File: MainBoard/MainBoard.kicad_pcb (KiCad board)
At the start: 6 copper layers, 45 x 45 mm, 4 parts, among them J2 USB4110-GF-A, J3 M55-7104042R

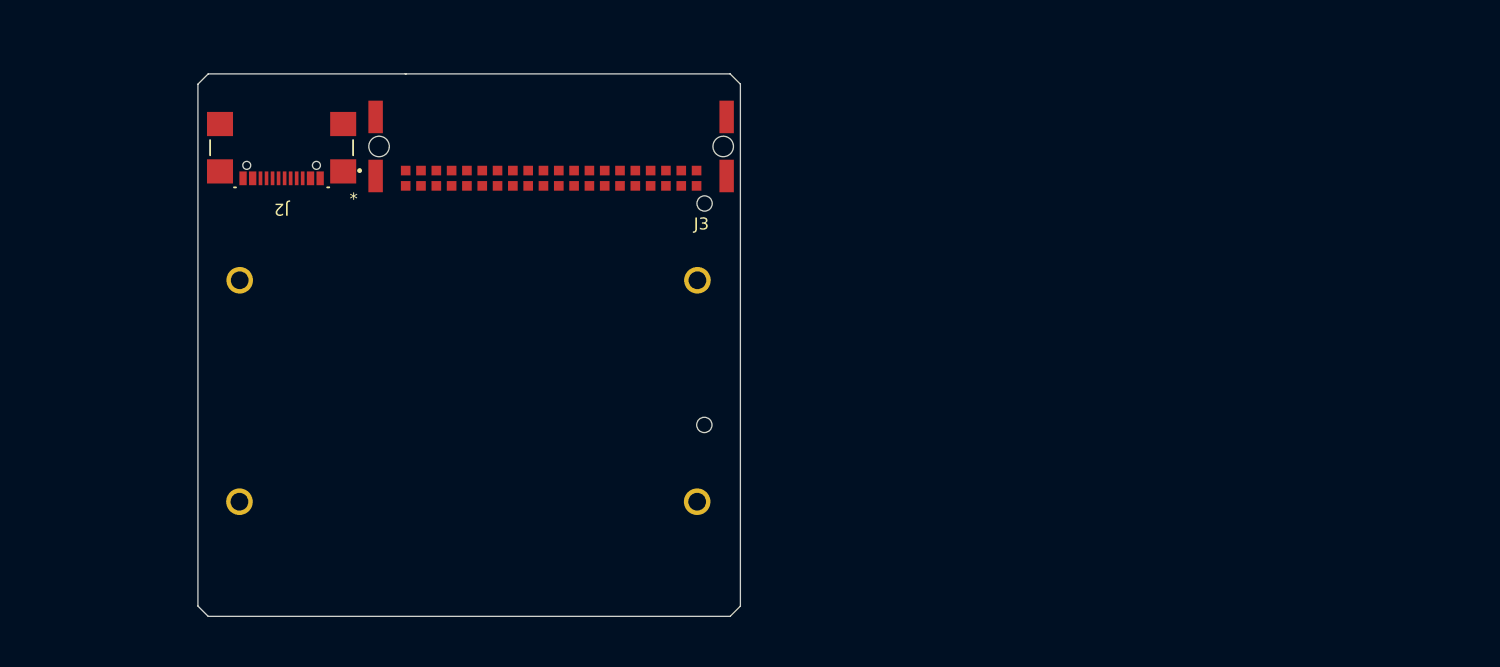
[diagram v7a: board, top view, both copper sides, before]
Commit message: Did some placement
Did most the caps for MCU, general placement for fill zones
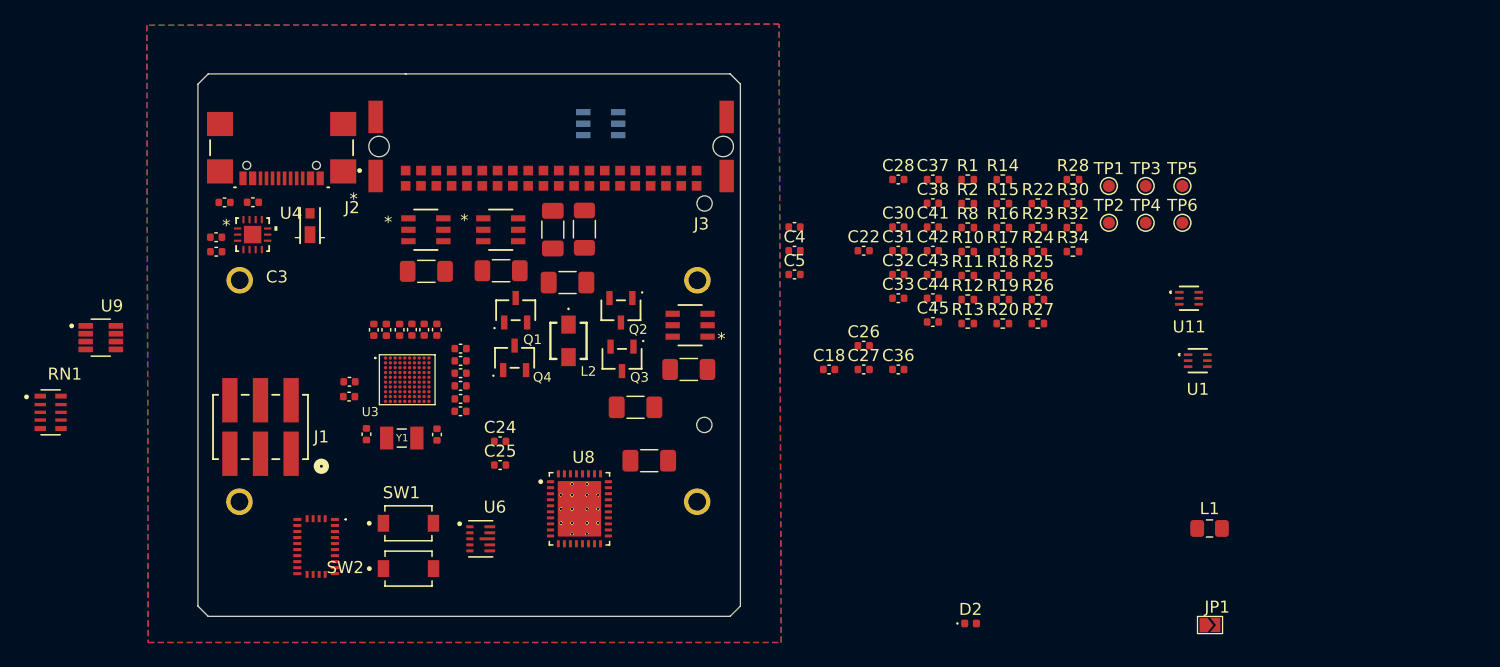
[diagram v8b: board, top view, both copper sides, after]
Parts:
- added C1: 1uF, Capacitor_SMD:C_0402_1005Metric, F.Cu at (70.9, 55.3)
- added C10: 4.7uF, Capacitor_SMD:C_0402_1005Metric, F.Cu at (85.0, 63.0)
- added C11: 4.7uF, Capacitor_SMD:C_0402_1005Metric, F.Cu at (87.2, 63.0)
- added C12: 100nF, Capacitor_SMD:C_0402_1005Metric, F.Cu at (89.2, 63.0)
- added C13: 100nF, Capacitor_SMD:C_0402_1005Metric, F.Cu at (88.2, 63.0)
- added C14: 100nF, Capacitor_SMD:C_0402_1005Metric, F.Cu at (91.2, 64.5)
- added C15: 100nF, Capacitor_SMD:C_0402_1005Metric, F.Cu at (82.0, 67.3)
- added C16: 1uF, Capacitor_SMD:C_0402_1005Metric, F.Cu at (84.0, 63.0)
- added C17: 100nF, Capacitor_SMD:C_0402_1005Metric, F.Cu at (81.9, 68.5)
- added C18: 10uF, Capacitor_SMD:C_0402_1005Metric, F.Cu at (121.8, 66.3)
- added C19: 1uF, Capacitor_SMD:C_0402_1005Metric, F.Cu at (91.2, 65.6)
- added C2: 100nF, Capacitor_SMD:C_0402_1005Metric, F.Cu at (70.9, 56.5)
- added C20: 100nF, Capacitor_SMD:C_0402_1005Metric, F.Cu at (86.1, 63.0)
- added C21: 100nF, Capacitor_SMD:C_0402_1005Metric, F.Cu at (91.2, 66.6)
- added C22: 100nF, Capacitor_SMD:C_0402_1005Metric, F.Cu at (124.6, 56.4)
- added C23: 100nF, Capacitor_SMD:C_0402_1005Metric, F.Cu at (91.2, 67.6)
- added C24: 100nF, Capacitor_SMD:C_0402_1005Metric, F.Cu at (94.5, 72.2)
- added C25: 100nF, Capacitor_SMD:C_0402_1005Metric, F.Cu at (94.5, 74.2)
- added C26: 10uF, Capacitor_SMD:C_0402_1005Metric, F.Cu at (124.6, 64.3)
- added C27: 10uF, Capacitor_SMD:C_0402_1005Metric, F.Cu at (124.6, 66.3)
- added C28: 100nF, Capacitor_SMD:C_0402_1005Metric, F.Cu at (127.5, 50.5)
- added C29: 22pF, Capacitor_SMD:C_0402_1005Metric, F.Cu at (83.4, 71.7)
- added C3: 100nF, Capacitor_SMD:C_0402_1005Metric, F.Cu at (118.9, 54.5)
- added C30: 100nF, Capacitor_SMD:C_0402_1005Metric, F.Cu at (127.5, 54.5)
- added C31: 470nF, Capacitor_SMD:C_0402_1005Metric, F.Cu at (127.5, 56.4)
- added C32: 100nF, Capacitor_SMD:C_0402_1005Metric, F.Cu at (127.5, 58.4)
- added C33: 100nF, Capacitor_SMD:C_0402_1005Metric, F.Cu at (127.5, 60.4)
- added C34: 47uF, Capacitor_SMD:C_1206_3216Metric_Pad1.33x1.80mm_HandSolder, F.Cu at (105.7, 69.4)
- added C35: 47uF, Capacitor_SMD:C_1206_3216Metric_Pad1.33x1.80mm_HandSolder, F.Cu at (100.1, 59.1)
- added C36: 4.7uF, Capacitor_SMD:C_0402_1005Metric, F.Cu at (127.5, 66.3)
- added C37: 4.7uF, Capacitor_SMD:C_0402_1005Metric, F.Cu at (130.4, 50.5)
- added C38: 1uF, Capacitor_SMD:C_0402_1005Metric, F.Cu at (130.4, 52.5)
- added C39: 47uF, Capacitor_SMD:C_1206_3216Metric_Pad1.33x1.80mm_HandSolder, F.Cu at (106.8, 73.8)
- added C4: 100nF, Capacitor_SMD:C_0402_1005Metric, F.Cu at (118.9, 56.4)
- added C40: 47uF, Capacitor_SMD:C_1206_3216Metric_Pad1.33x1.80mm_HandSolder, F.Cu at (98.8, 54.7)
- added C41: 100nF, Capacitor_SMD:C_0402_1005Metric, F.Cu at (130.4, 54.5)
- added C42: 100nF, Capacitor_SMD:C_0402_1005Metric, F.Cu at (130.4, 56.4)
- added C43: 100nF, Capacitor_SMD:C_0402_1005Metric, F.Cu at (130.4, 58.4)
- added C44: 470nF, Capacitor_SMD:C_0402_1005Metric, F.Cu at (130.4, 60.4)
- added C45: 100nF, Capacitor_SMD:C_0402_1005Metric, F.Cu at (130.4, 62.3)
- added C46: 22pF, Capacitor_SMD:C_0402_1005Metric, F.Cu at (89.2, 71.7)
- added C5: 100nF, Capacitor_SMD:C_0402_1005Metric, F.Cu at (118.9, 58.4)
- added C6: 470pF, Capacitor_SMD:C_0402_1005Metric, F.Cu at (71.6, 52.4)
- added C7: 470pF, Capacitor_SMD:C_0402_1005Metric, F.Cu at (74.0, 52.4)
- added C8: 10nF, Capacitor_SMD:C_0402_1005Metric, F.Cu at (91.2, 68.7)
- added C9: 1uF, Capacitor_SMD:C_0402_1005Metric, F.Cu at (91.2, 69.8)
- added D1: MSS2P2-M3/89A, inspirefly:DIODE_MSP3V3, F.Cu at (78.7, 54.3)
- added D2: LED, LED_SMD:LED_0402_1005Metric, F.Cu at (133.5, 87.3)
- added J1: 0015912060 Molex, inspirefly:CONN_713080000-SD_06_M6p10_MOL, F.Cu at (74.6, 71.0)
- added JP1: Footswitch_Disable, inspirefly:SmallJumper, F.Cu at (153.3, 87.5)
- added L1: 470nH, Inductor_SMD:L_0805_2012Metric_Pad1.15x1.40mm_HandSolder, F.Cu at (153.3, 79.5)
- added L2: 2.2uH, inspirefly:IHLP1212BZEZ2R2M1Z, F.Cu at (100.1, 63.9)
- added Q1: PMV19XNEAR, inspirefly:TO-236AB_SOT23_NEX, F.Cu at (95.8, 61.4)
- added Q2: PMV19XNEAR, inspirefly:TO-236AB_SOT23_NEX, F.Cu at (104.5, 61.4)
- added Q3: PMV19XNEAR, inspirefly:TO-236AB_SOT23_NEX, F.Cu at (104.6, 65.4)
- added Q4: PMV19XNEAR, inspirefly:TO-236AB_SOT23_NEX, F.Cu at (95.7, 65.3)
- added R1: 1k, Resistor_SMD:R_0402_1005Metric, F.Cu at (133.3, 50.5)
- added R10: 10k, Resistor_SMD:R_0402_1005Metric, F.Cu at (133.3, 56.5)
- added R11: 280k, Resistor_SMD:R_0402_1005Metric, F.Cu at (133.3, 58.5)
- added R12: 50k, Resistor_SMD:R_0402_1005Metric, F.Cu at (133.3, 60.5)
- added R13: 100K, Resistor_SMD:R_0402_1005Metric, F.Cu at (133.3, 62.5)
- added R14: 143k, Resistor_SMD:R_0402_1005Metric, F.Cu at (136.2, 50.5)
- added R15: 250k, Resistor_SMD:R_0402_1005Metric, F.Cu at (136.2, 52.5)
- added R16: 6.2k, Resistor_SMD:R_0402_1005Metric, F.Cu at (136.2, 54.5)
- added R17: 36k, Resistor_SMD:R_0402_1005Metric, F.Cu at (136.2, 56.5)
- added R18: 10, Resistor_SMD:R_0402_1005Metric, F.Cu at (136.2, 58.5)
- added R19: 50k, Resistor_SMD:R_0402_1005Metric, F.Cu at (136.2, 60.5)
- added R2: 1k, Resistor_SMD:R_0402_1005Metric, F.Cu at (133.3, 52.5)
- added R20: 40k, Resistor_SMD:R_0402_1005Metric, F.Cu at (136.2, 62.5)
- added R21: 5m, Resistor_SMD:R_1206_3216Metric_Pad1.30x1.75mm_HandSolder, F.Cu at (101.5, 54.6)
- added R22: 100k, Resistor_SMD:R_0402_1005Metric, F.Cu at (139.1, 52.5)
- added R23: 10, Resistor_SMD:R_0402_1005Metric, F.Cu at (139.1, 54.5)
- added R24: 10k, Resistor_SMD:R_0402_1005Metric, F.Cu at (139.1, 56.5)
- added R25: 120, Resistor_SMD:R_0402_1005Metric, F.Cu at (139.1, 58.5)
- added R26: 10k, Resistor_SMD:R_0402_1005Metric, F.Cu at (139.1, 60.5)
- added R27: 10, Resistor_SMD:R_0402_1005Metric, F.Cu at (139.1, 62.5)
- added R28: 10, Resistor_SMD:R_0402_1005Metric, F.Cu at (142.0, 50.5)
- added R29: 5m, Resistor_SMD:R_1206_3216Metric_Pad1.30x1.75mm_HandSolder, F.Cu at (110.1, 66.3)
- added R30: 10, Resistor_SMD:R_0402_1005Metric, F.Cu at (142.0, 52.5)
- added R31: 5m, Resistor_SMD:R_1206_3216Metric_Pad1.30x1.75mm_HandSolder, F.Cu at (88.3, 58.1)
- added R32: 100K, Resistor_SMD:R_0402_1005Metric, F.Cu at (142.0, 54.5)
- added R33: 5m, Resistor_SMD:R_1206_3216Metric_Pad1.30x1.75mm_HandSolder, F.Cu at (94.5, 58.1)
- added R34: 100K, Resistor_SMD:R_0402_1005Metric, F.Cu at (142.0, 56.5)
- added R8: 2.2k, Resistor_SMD:R_0402_1005Metric, F.Cu at (133.3, 54.5)
- added RN1: YC158TJR-072K2L, inspirefly:RESCAXE64P320X160X70-10N, F.Cu at (57.2, 69.8)
- added SW1: SW_TL1015AF160QG, inspirefly:SW_TL1015AF160QG, F.Cu at (86.9, 79.0)
- added SW2: SW_TL1015AF160QG, inspirefly:SW_TL1015AF160QG, F.Cu at (86.9, 82.8)
- added TP1: BatBeforeCutoff, TestPoint:TestPoint_Pad_D1.0mm, F.Cu at (145.0, 51.1)
- added TP2: Bat+, TestPoint:TestPoint_Pad_D1.0mm, F.Cu at (145.0, 54.1)
- added TP3: 3.3V, TestPoint:TestPoint_Pad_D1.0mm, F.Cu at (148.0, 51.1)
- added TP4: GND, TestPoint:TestPoint_Pad_D1.0mm, F.Cu at (148.0, 54.1)
- added TP5: GND, TestPoint:TestPoint_Pad_D1.0mm, F.Cu at (151.1, 51.1)
- added TP6: GND, TestPoint:TestPoint_Pad_D1.0mm, F.Cu at (151.1, 54.1)
- added U1: INA185A4IDRLR, inspirefly:SOT_INA185_TEX, F.Cu at (152.3, 65.6)
- added U10: SI3477DV-T1-GE3, inspirefly:SOT_V-T1-GE3_VIS-M, F.Cu at (88.3, 54.7)
- added U11: INA185A4IDRLR, inspirefly:SOT_INA185_TEX, F.Cu at (151.6, 60.4)
- added U12: SI3477DV-T1-GE3, inspirefly:SOT_V-T1-GE3_VIS-M, F.Cu at (94.5, 54.7)
- added U2: SI3477DV-T1-GE3, inspirefly:SOT_V-T1-GE3_VIS-M, B.Cu at (102.8, 45.9)
- added U3: STM32L496VGY6PTR, inspirefly:STM32L496VGY6TR, F.Cu at (86.8, 67.1)
- added U4: FUSB302BMPX, inspirefly:MLP14_2P5X2P5_ONS, F.Cu at (73.9, 55.1)
- added U5: BNO086, inspirefly:BNO086, F.Cu at (79.2, 81.0)
- added U6: TPS63802DLAR, inspirefly:VREG_TPS63802DLAR, F.Cu at (92.9, 80.3)
- added U7: SI3477DV-T1-GE3, inspirefly:SOT_V-T1-GE3_VIS-M, F.Cu at (110.2, 62.6)
- added U8: BQ25756ERRVR, inspirefly:IC_BQ25756ERRVR, F.Cu at (101.0, 77.8)
- added U9: TCAN332DCNR, inspirefly:SOT65P280X145-8N, F.Cu at (61.3, 63.6)
- added Y1: XTAL_ABS07-32.768KHZ-T, inspirefly:XTAL_ABS07-32.768KHZ-T, F.Cu at (86.3, 72.0)
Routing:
- added copper zone on In3.Cu, net +3.3V
- added copper zone on B.Cu, net GND
- added copper zone on F.Cu, net GND
- added copper zone on In1.Cu, net GND
- added copper zone on In2.Cu, net GND
- added copper zone on In4.Cu, net GND
